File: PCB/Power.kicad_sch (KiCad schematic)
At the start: 12 parts, among them J4 Conn_01x02, U1 MCP73831-2-OT, U10 AMS1117-3.3, U9 MAX17048G

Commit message: Restarted the schematic
It was getting way to full.
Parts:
- removed C2: 100nF, Capacitor_SMD:C_0603_1608Metric, symbol Device:C_Small
- removed C21: 22uF, Capacitor_SMD:C_0603_1608Metric, symbol Device:C_Small
- removed C5: 4.7nF, Capacitor_SMD:C_0603_1608Metric, symbol Device:C_Small
- removed C6: 1uF, Capacitor_SMD:C_0603_1608Metric, symbol Device:C_Small
- removed C7: 10uF, Capacitor_SMD:C_0603_1608Metric, symbol Device:C_Small
- removed D5: LED, LED_SMD:LED_0805_2012Metric, symbol Device:LED
- removed J4: Conn_01x02, Connector_JST:JST_PH_S2B-PH-K_1x02_P2.00mm_Horizontal, symbol Connector_Generic:Conn_01x02
- removed R12: 470, Resistor_SMD:R_0201_0603Metric, symbol Device:R_US
- removed R13: 1k, Resistor_SMD:R_0201_0603Metric, symbol Device:R_US
- removed U1: MCP73831-2-OT, Package_TO_SOT_SMD:SOT-23-5, symbol Battery_Management:MCP73831-2-OT
- removed U10: AMS1117-3.3, Package_TO_SOT_SMD:SOT-223-3_TabPin2, symbol Regulator_Linear:AMS1117-3.3
- removed U9: MAX17048G, Package_DFN_QFN:TDFN-8-1EP_2x2mm_P0.5mm_EP0.8x1.2mm, symbol CustomSymbols:MAX17048G
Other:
- company: (none) -> Joshua E
- title: (none) -> Music Player

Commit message: Add power supply symbols to Power schematic
Added standard library symbols for connectors, capacitors, Schottky diodes, inductors, resistors, linear and switching regulators, and power rails (+3V3, +5V, +BATT, GND, VBUS) to Power.kicad_sch. Also made minor adjustments to sheet page assignments in MusicPlayer.kicad_sch and reordered a section in MusicPlayer.kicad_pro.
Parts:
- added C1, C4: 22u, symbol Device:C
- added C2: 120p, symbol Device:C
- added C3: 10u, symbol Device:C
- added D1: SS12, Diode_SMD:D_SMA, symbol Diode:SS12
- added D2, D3: 300mV, symbol Device:D_Schottky
- added J1: 3.7v LiPo, symbol Connector:Conn_01x02_Socket
- added L1: 2.2u, symbol Device:L_Iron
- added R1: R, symbol Device:R
- added U1: TPS613221ADBV, Package_TO_SOT_SMD:SOT-23-5, symbol Regulator_Switching:TPS613221ADBV
- added U2: AMS1117-3.3, Package_TO_SOT_SMD:SOT-223-3_TabPin2, symbol Regulator_Linear:AMS1117-3.3
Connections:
- new net: C2.1, R1.2
- new net: D1.2 (A), L1.2, R1.1, U1.1 (SW)
- new net: C3.2, D2.1 (K), D3.1 (K), U2.3 (VI)
- new net +3V3: C4.2, U2.2 (VO)
- new net +5V: C1.1, C2.2, D1.1 (K), D2.2 (A), U1.4 (VOUT)
- new net +BATT: J1.1 (Pin_1), L1.1
- new net GND: C1.2, C3.1, C4.1, J1.2 (Pin_2), U1.2 (GND), U2.1 (GND)
- new net VBUS: D3.2 (A)

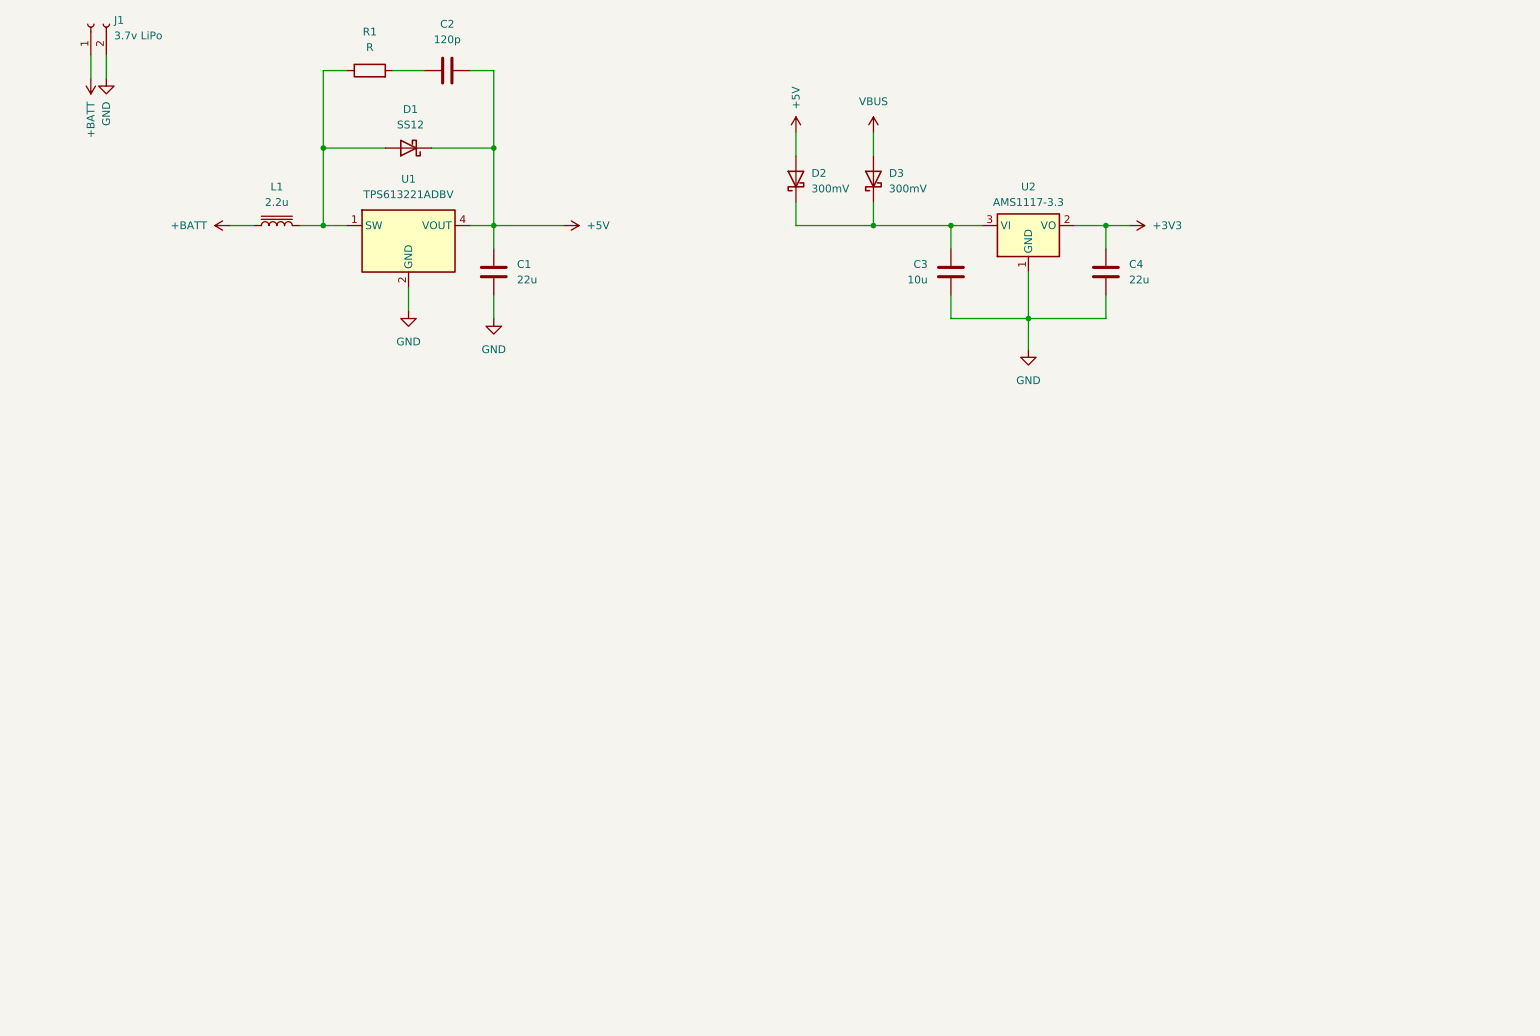
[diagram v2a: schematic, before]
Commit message: Update Power schematic with new symbols and components
Replaced and added several symbols in Power.kicad_sch, including MCP73831-2-OT battery charger, TPS61090 boost converter, and updated passive components (LED, capacitor, inductor, resistor). Adjusted symbol properties, footprints, and pinouts to match new components. Updated schematic text, junctions, and added descriptive notes for charge rate and low battery voltage. Minor tweaks to MusicPlayer.kicad_sch sheet positions and grouping in MusicPlayer.kicad_pro.
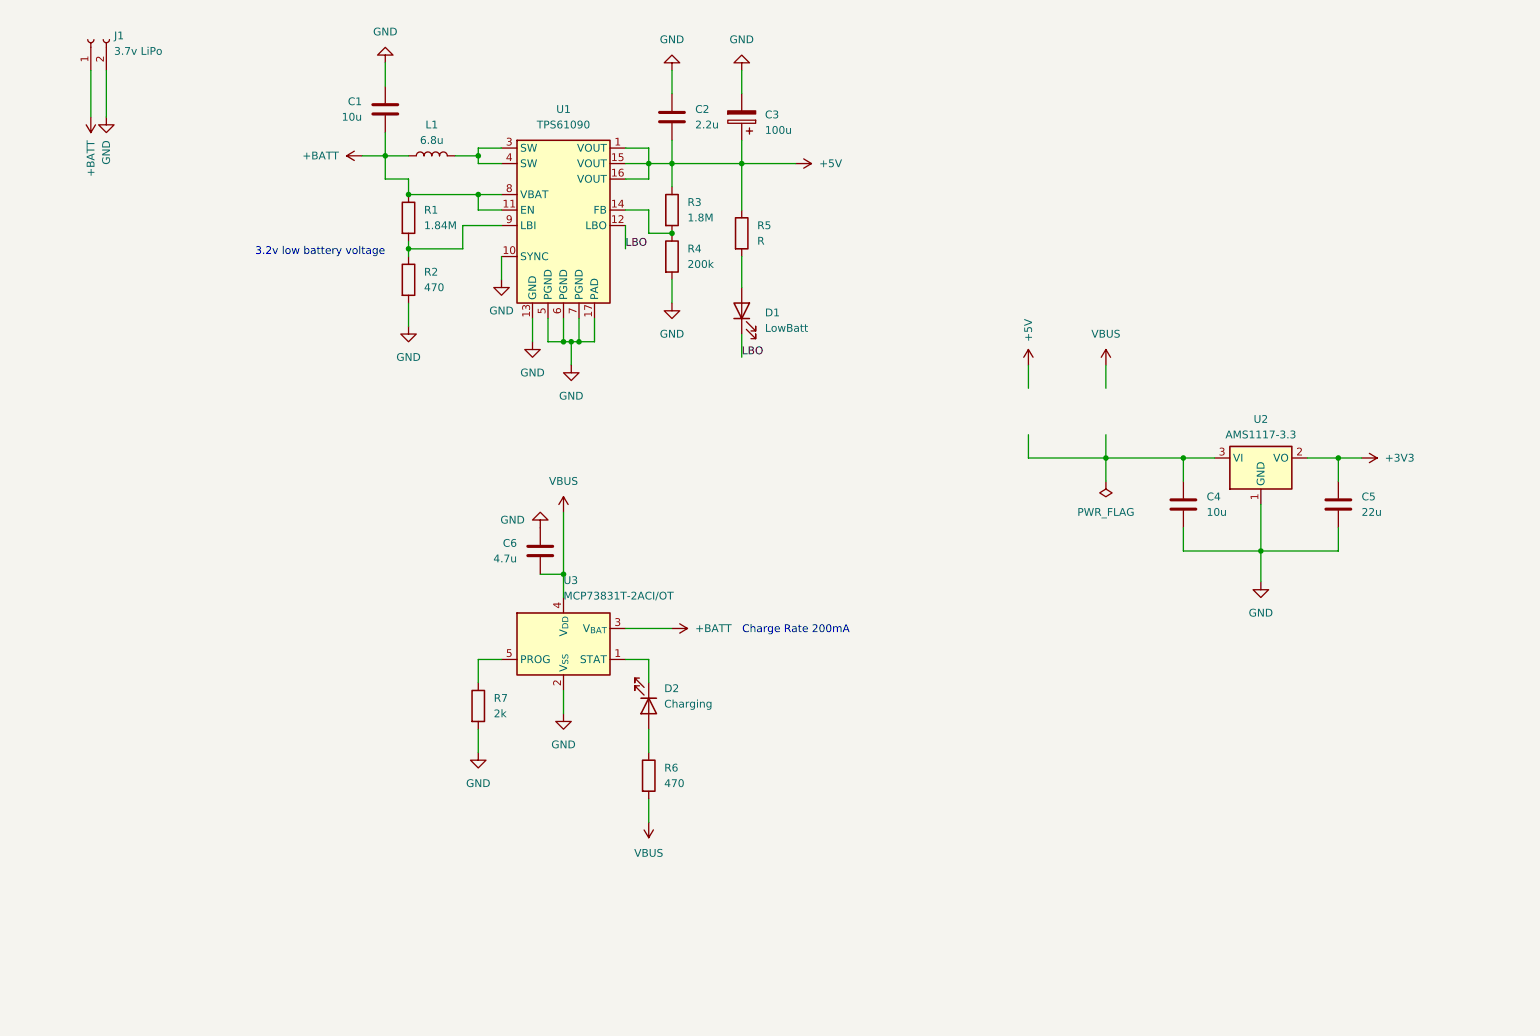
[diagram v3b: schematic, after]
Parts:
- removed C3: 10u, symbol Device:C
- removed D1: SS12, Diode_SMD:D_SMA, symbol Diode:SS12
- removed D2, D3: 300mV, symbol Device:D_Schottky
- removed L1: 2.2u, symbol Device:L_Iron
- removed U1: TPS613221ADBV, Package_TO_SOT_SMD:SOT-23-5, symbol Regulator_Switching:TPS613221ADBV
- added C3: 100u, Capacitor_SMD:C_0201_0603Metric, symbol Device:C_Polarized
- added C5: 22u, Capacitor_SMD:C_0201_0603Metric, symbol Device:C
- added C6: 4.7u, Capacitor_SMD:C_0201_0603Metric, symbol Device:C
- added D1: LowBatt, LED_SMD:LED_0201_0603Metric, symbol Device:LED
- added D2: Charging, LED_SMD:LED_0201_0603Metric, symbol Device:LED
- added L1: 6.8u, symbol Device:L
- added R3: 1.8M, Resistor_SMD:R_0201_0603Metric, symbol Device:R
- added R4: 200k, Resistor_SMD:R_0201_0603Metric, symbol Device:R
- added R5: R, Resistor_SMD:R_0201_0603Metric, symbol Device:R
- added R6: 470, Resistor_SMD:R_0201_0603Metric, symbol Device:R
- added R7: 2k, Resistor_SMD:R_0201_0603Metric, symbol Device:R
- added U1: TPS61090, Package_DFN_QFN:Texas_RSA_VQFN-16-1EP_4x4mm_P0.65mm_EP2.7x2.7mm_ThermalVias, symbol Regulator_Switching:TPS61090
- added U3: MCP73831T-2ACI/OT, Package_TO_SOT_SMD:SOT-23-5, symbol Battery_Management:MCP73831-2-OT
- C1, C4: value 22u -> 10u; footprint (none) -> Capacitor_SMD:C_0201_0603Metric
- C2: value 120p -> 2.2u; footprint (none) -> Capacitor_SMD:C_0201_0603Metric
- J1: footprint (none) -> Connector_JST:JST_PH_S2B-PH-K_1x02_P2.00mm_Horizontal
- R1: value R -> 1.84M; footprint (none) -> Resistor_SMD:R_0201_0603Metric
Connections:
- net +3V3: now also C5.1; no longer C4.2
- net +5V: now also C3.1, R3.1, R5.1, U1.1 (VOUT), U1.15 (VOUT), U1.16 (VOUT); no longer C1.1
- net +BATT: now also C1.2, R1.1, L1.1, U1.11 (EN), U1.8 (VBAT), U3.3 (V_{BAT})
- net GND: now also C1.1, C2.1, C4.2, C3.2, C5.2, C6.1, R4.2, R6.2, R7.2, U1.10 (SYNC), U1.13 (GND), U1.17 (PAD), U1.5 (PGND), U1.6 (PGND), U1.7 (PGND), U3.2 (V_{SS}); no longer C1.2, C4.1
- net VBUS: now also C6.2, R6.2, U3.4 (V_{DD})
- net at R1.2: now also R6.1, U1.9 (LBI); no longer C2.1
- net at U2.3 (VI): now also C4.1
- new net: R7.1, U3.5 (PROG)
- new net: L1.2, U1.3 (SW), U1.4 (SW)
- new net: R3.2, R4.1, U1.14 (FB)
- new net: D2.2 (A), R6.1
- new net: D2.1 (K), U3.1 (STAT)
- new net: D1.2 (A), R5.2
- new net LBO: D1.1 (K), U1.12 (LBO)
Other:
- note added: "3.2v low battery voltage"
- note added: "Charge Rate 200mA"
- moved on the sheet: J1, U2

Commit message: Add components & update KiCad schematic settings
Add and refine schematic symbols and project settings across PCB files. Inputs.kicad_sch: expand library symbols and instances (resistor, SPDT switch, power flags, GND, wiring and global labels). Power.kicad_sch: add a Schottky diode symbol, replace/regenerate regulator symbol (rename to LD1117S33TR_SOT223 and update datasheet/description/keywords), and add simulation transistor symbols (NMOS, PNP) with Sim.* properties and updated graphics. MusicPlayer.kicad_pro: tighten lib_symbol_mismatch to error, adjust BOM settings (exclude_dnp true, show quantity, hide DNP/Exclude fields, add/hide Sim.Device/Sim.Type fields) and change BOM sorting to Reference ascending. These changes improve symbol definitions for simulation, ERC/BOM accuracy, and project export settings.
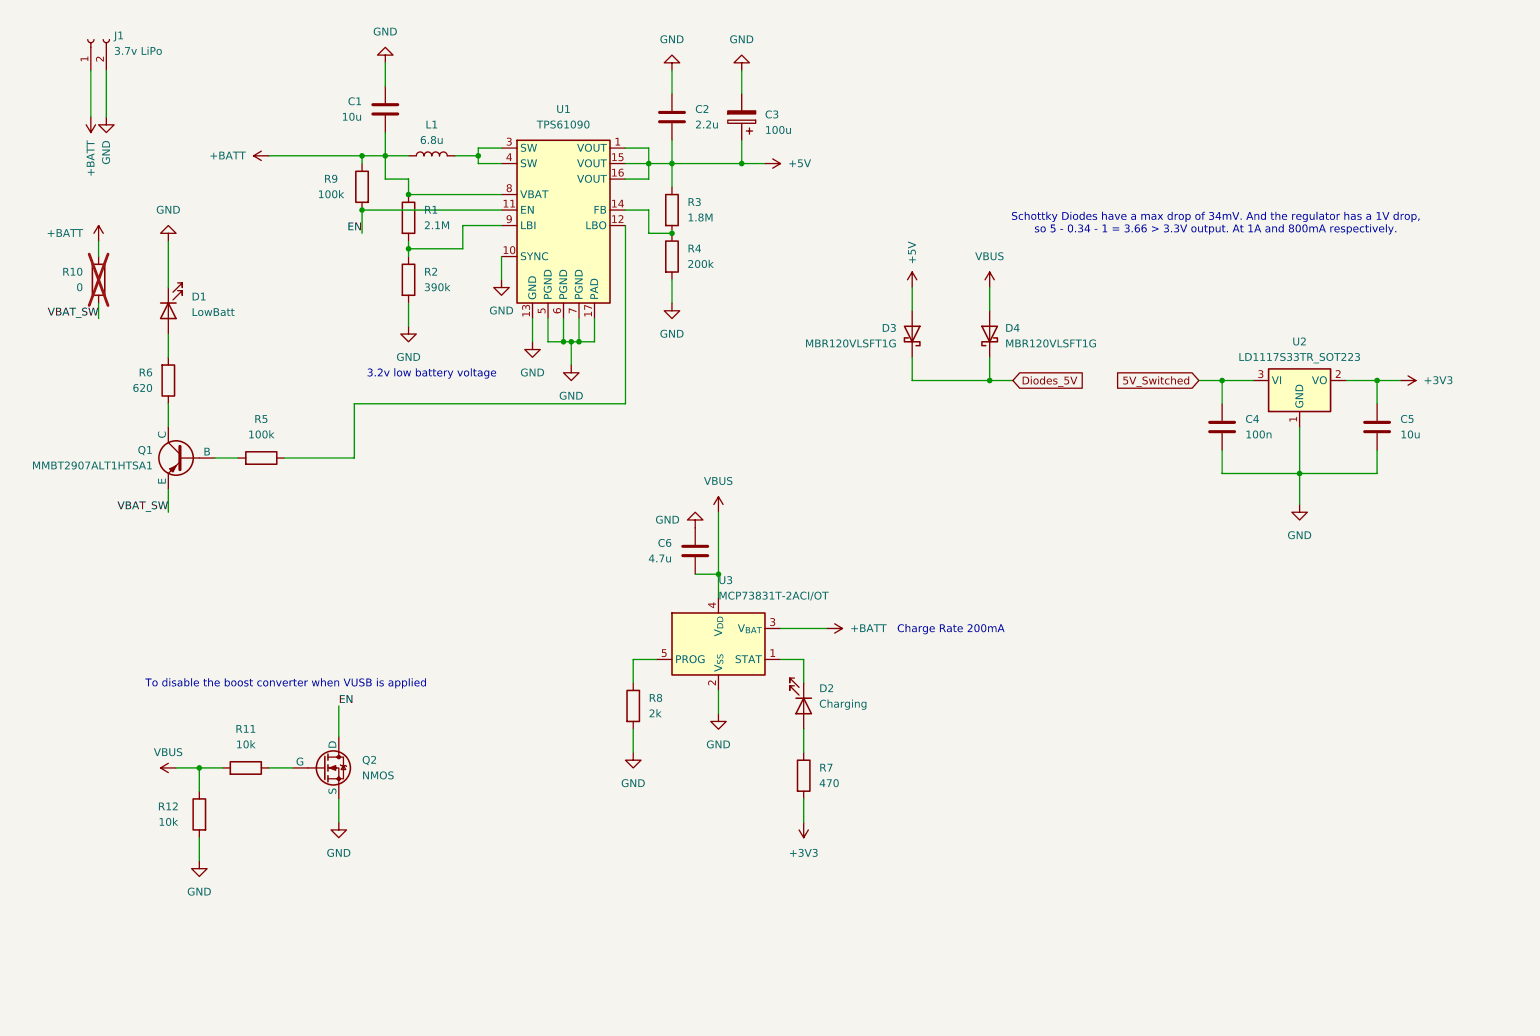
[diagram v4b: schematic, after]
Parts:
- removed U2: AMS1117-3.3, Package_TO_SOT_SMD:SOT-223-3_TabPin2, symbol Regulator_Linear:AMS1117-3.3
- added D3, D4: MBR120VLSFT1G, CustomFootprints:D_SOD-123FL, symbol Device:D_Schottky
- added Q1: MMBT2907ALT1HTSA1, Package_TO_SOT_SMD:SOT-23, symbol Simulation_SPICE:PNP
- added Q2: NMOS, Package_TO_SOT_SMD:SOT-23, symbol Simulation_SPICE:NMOS
- added R10: 0, Resistor_SMD:R_0201_0603Metric, symbol Device:R
- added R11, R12: 10k, Resistor_SMD:R_0201_0603Metric, symbol Device:R
- added R6: 620, Resistor_SMD:R_0201_0603Metric, symbol Device:R
- added R7: 470, Resistor_SMD:R_0201_0603Metric, symbol Device:R
- added R9: 100k, Resistor_SMD:R_0201_0603Metric, symbol Device:R
- added U2: LD1117S33TR_SOT223, Package_TO_SOT_SMD:SOT-223-3_TabPin2, symbol Regulator_Linear:LD1117S33TR_SOT223
- C1: LCSC (none) -> C1691
- C2: LCSC (none) -> C23630
- C3: footprint Capacitor_SMD:C_0201_0603Metric -> Capacitor_SMD:CP_Elec_10x10; LCSC (none) -> C2163037
- C4: value 10u -> 100n; LCSC (none) -> C1590
- C5: value 22u -> 10u; LCSC (none) -> C1691
- C6: LCSC (none) -> C1705
- D1: LCSC (none) -> C83242
- D2: LCSC (none) -> C5184984
- J1: LCSC (none) -> C173752
- L1: footprint (none) -> CustomFootprints:L_10.2x10; LCSC (none) -> C167253
- R1: value 1.84M -> 2.1M; LCSC (none) -> C2085910
- R2: renamed from R6; value 470 -> 390k; LCSC (none) -> C2074176
- R3: LCSC (none) -> C3151701
- R4: LCSC (none) -> C844339
- R5: value R -> 100k; LCSC (none) -> C844888
- R8: renamed from R7; LCSC (none) -> C313719
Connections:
- net +3V3: now also R7.2, U2.2 (VO)
- net +5V: now also D3.2 (A); no longer R5.1
- net +BATT: now also R10.2, R9.1; no longer U1.11 (EN)
- net GND: now also D1.1 (K), Q2.3 (S), R12.2, U2.1 (GND)
- net VBUS: now also D4.2 (A), R11.2, R12.1; no longer R2.2
- net 5V_Switched: now reaches C4.1
- net 5V_Switched: now also U2.3 (VI)
- net at D2.2 (A): now also R7.1; no longer R2.1
- net at R5.2: now also Q1.2 (B); no longer D1.2 (A)
- net LBO: no longer names the net of U1.12 (LBO)
- net LBO: now also R5.1; no longer D1.1 (K)
- new net: Q2.2 (G), R11.1
- new net: Q1.1 (C), R6.1
- new net: D1.2 (A), R6.2
- new net Diodes_5V: D3.1 (K), D4.1 (K)
- new net EN: Q2.1 (D), R9.2, U1.11 (EN)
- new net VBAT_SW: Q1.3 (E), R10.1
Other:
- note added: "Schottky Diodes have a max drop of 34mV. And the regulator has a 1V drop, so 5 - 0.34 - 1 = 3.66 > 3.3V output. At 1A and 800mA respectively."
- note added: "To disable the boost converter when VUSB is applied"
- moved on the sheet: C4, C5, C6, D1, D2, R8, U3

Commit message: Finished the schematic.
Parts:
- removed C4: 100n, Capacitor_SMD:C_0201_0603Metric, symbol Device:C
- added C16: 100n, Capacitor_SMD:C_0201_0603Metric, symbol Device:C
- added R23: 10k, Resistor_SMD:R_0201_0603Metric, symbol Device:R
- added U6: MAX17048G, Package_DFN_QFN:TDFN-8-1EP_2x2mm_P0.5mm_EP0.8x1.2mm, symbol CustomSymbols:MAX17048G
- R7: value 470 -> 1.07k; LCSC C844786 -> C4217127
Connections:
- net +3V3: now also R23.1; no longer R7.2
- net +BATT: now also C16.2, U6.2 (CELL), U6.3 (VDD)
- net 5V_Switched: now also C16.1
- net GND: now also C16.1, C16.2, U6.1 (CTG), U6.4 (GND), U6.6 (QSTRT), U6.9 (EP)
- net VBUS: now also R7.2
- new net ALRT: R23.2, U6.5 (ALRT)
- new net SCL: U6.7 (SCL)
- new net SDA: U6.8 (SDA)
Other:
- moved on the sheet: C5, C6, D2, D3, D4, Q2, R11, R12, R8, U2, U3

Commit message: Finale touch up on schematics
Added net classes and did set the pcb configuration values.
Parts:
- added C16: 100n, Capacitor_SMD:C_0201_0603Metric, symbol Device:C
- renumbered C16 to C4
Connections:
- net +BATT: now also C16.2; no longer C4.2
- net GND: now also C16.1; no longer C4.1
